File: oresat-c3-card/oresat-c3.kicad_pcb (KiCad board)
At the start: 4 copper layers, 99.8 x 94.6 mm, 517 parts, among them J1 TFM-120-01-L-D-RA, J3 733000020, J4 733000020, J5 DM3BT-DSF-PEJS, J6 Conn_01x02, J8 SM14B-SHLS-TF, Q1 NTR4101P, Q3 NTR4101P, Q4 PMV45EN, Q6 MMBT2907, U1 OSD3358-1G-ISM, U10 SN74AUC1G07DCKR, U11 RCLAMP0504FB, U12 RCLAMP0504FB, U13 MAX892LEUA+T, U14 TLVH431, U15 Qorvo 856930, U16 AT86RF215, U17 SI4112-GM, U18 LT5534, U19 BDCN-20-13+, U2 BP0805A1308, U20 QPC1022, U21 TQP7M9105, U22 LT5534, U23 NCS2-62+, U24 RV-3028-C7, U25 SN74LVC1G11IDCKRQ1, U26 TLV7041DBV, U27 SN74LVC1G04DCKR, U28 TLV1704-SEP, U29 TQP3M9036, U3 BP0805A1308, U30 FM24CL64B-GTR, U31 LP2985AIM5-3.3, U32 SF2446E, U33 SF2446E, U34 TPS259621DDA, U35 TPS259620DDA, U36 LTC3624-5, U37 LTC4300A-1, U38 LP2985AIM5-3.3, U39 TCAN330, U4 BGB741L7ESD, U40 MAX941EUA+, U41 TQP3M9036, U44 AT86RF215, U45 NCS2-62+, U47 QPC1022, U5 BP0805A1308, U6 LTC3624-5, U7 MAC-24+, U8 TCAN330, U9 SFEM016GB1EA1TO-I-GE-121-STD, X1 TXETALSANF-26.000000, X3 TXETALSANF-26.000000, Y1 ECS-240-12-30BQ-AEN-TR, Y2 ABS07-32.768KHZ-T

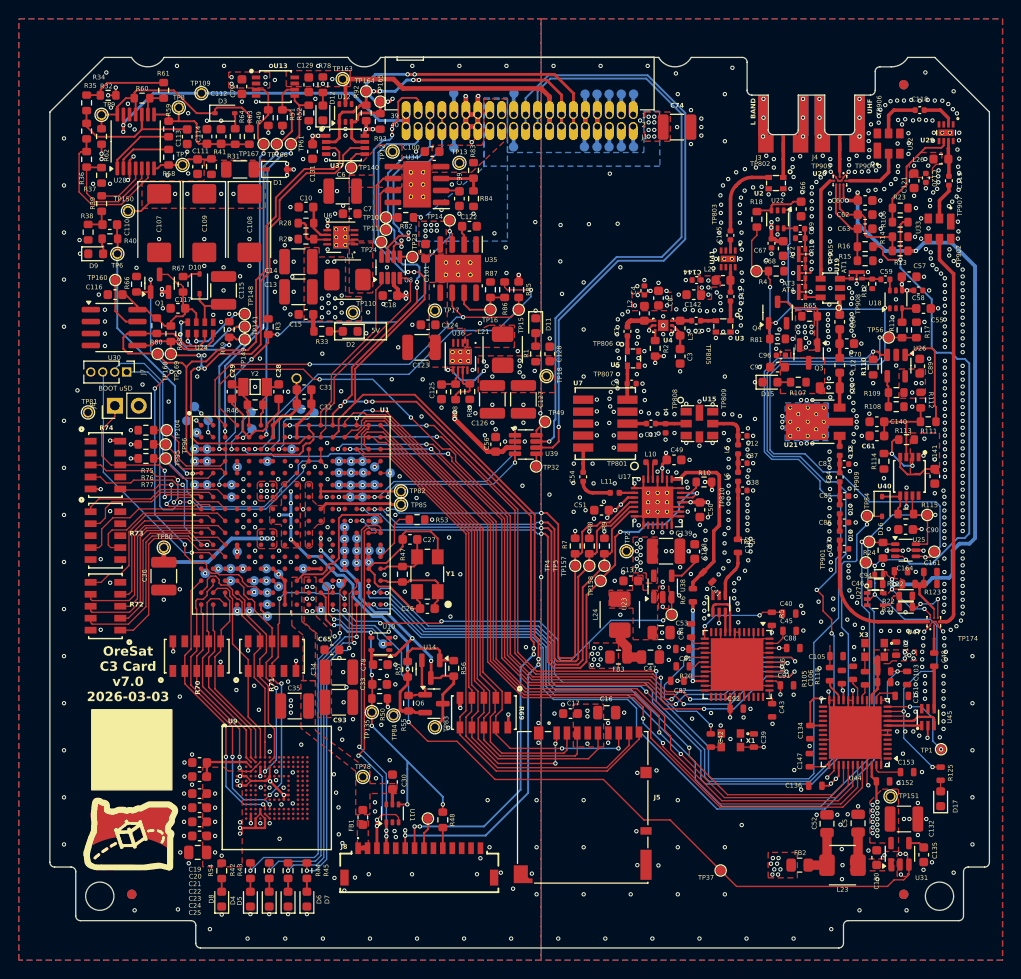
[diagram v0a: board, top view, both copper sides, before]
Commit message: Design review on C3 v7.0
Glenn and Andrew did a design review. Removed fiducials on back of board. Lots of schematic fixes, including
direction connection of TCXOs to AT86s, corrected LPF of CLKO from AT86 to the synth reference, fixed drive
levels both QPC switches in UHF radio, confirmed QPC directions, and some minor polishing.
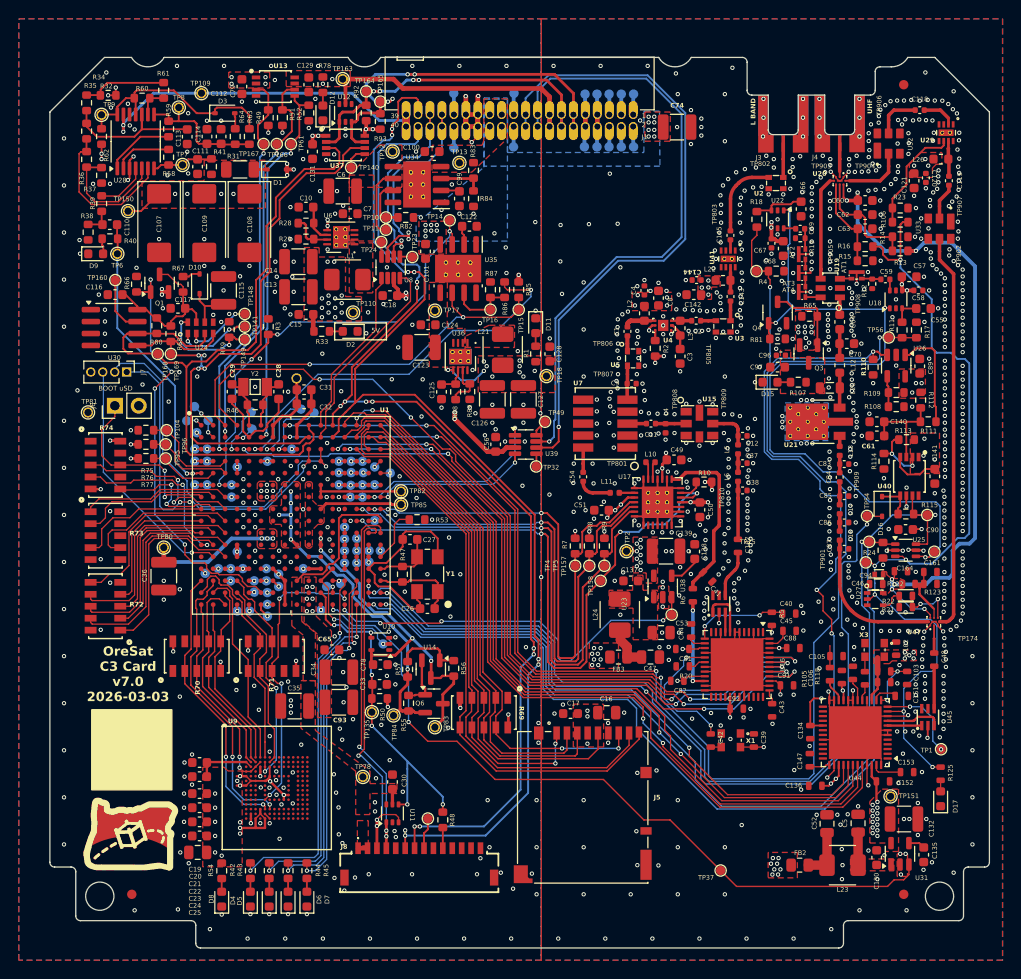
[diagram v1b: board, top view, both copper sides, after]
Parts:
- removed FB1: BLM18KG300JH1D, Inductor_SMD:L_0603_1608Metric
- removed FID4, FID5, FID6: Fiducial, Fiducial:Fiducial_1mm_Mask2mm
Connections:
- net SPARE31 renamed Net-(J1-Pad31)
- net SPARE32 renamed Net-(J1-Pad32)
- J8 pad 1: Net-(FB1-Pad1) -> VIN_USB
- J8 pad 2: Net-(FB1-Pad1) -> VIN_USB
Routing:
- net VIN_USB: track 16.5 -> 17.5 mm
- net Net-(FB1-Pad1): track 1.00 -> 0.00 mm
- removed copper zone on F.Cu, net Net-(FB1-Pad1)
